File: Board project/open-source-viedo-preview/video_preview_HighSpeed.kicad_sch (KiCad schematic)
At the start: 1 part, among them J6 Conn_01x22_Female

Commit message: 150-200 pin's created by Mateusz
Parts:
- added J15, J16, J5: Conn_01x22_Female, Connector_FFC-FPC:Hirose_FH12-22S-0.5SH_1x22-1MP_P0.50mm_Horizontal, symbol Connector:Conn_01x22_Female
- added J? (x2): HDMI_A_1.4, symbol Connector:HDMI_A_1.4
- added Module?: ComputeModule4-CM4, CM4IO:Raspberry-Pi-4-Compute-Module, symbol RPI_CM4_video_preview:ComputeModule4-CM4
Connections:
- net +3.3V: now also J16.22 (Pin_22)
- net CAM_GPIO: now also J5.17 (Pin_17)
- net GND: now also J15.1 (Pin_1), J15.10 (Pin_10), J15.13 (Pin_13), J15.16 (Pin_16), J15.19 (Pin_19), J15.4 (Pin_4), J15.7 (Pin_7), J16.1 (Pin_1), J16.10 (Pin_10), J16.13 (Pin_13), J16.16 (Pin_16), J16.19 (Pin_19), J16.4 (Pin_4), J16.7 (Pin_7), J5.1 (Pin_1), J5.10 (Pin_10), J5.13 (Pin_13), J5.16 (Pin_16), J5.4 (Pin_4), J5.7 (Pin_7), J?.11 (CKS), J?.11 (CKS), J?.17 (GND), J?.17 (GND), J?.2 (D2S), J?.2 (D2S), J?.5 (D1S), J?.5 (D1S), J?.8 (D0S), J?.8 (D0S), J?.SH, J?.SH
- net SCL0: now also J16.20 (Pin_20)
- net SDA0: now also J16.21 (Pin_21)
- new net: Module?.150 (GND), Module?.156 (GND), Module?.162 (GND), Module?.168 (GND), Module?.174 (GND), Module?.180 (GND), Module?.186 (GND), Module?.192 (GND), Module?.198 (GND)
- new net: Module?.155 (GND), Module?.161 (GND), Module?.167 (GND), Module?.173 (GND), Module?.179 (GND), Module?.185 (GND), Module?.191 (GND), Module?.197 (GND)
- new net +3.3v: J15.22 (Pin_22), J5.22 (Pin_22)
- new net CAM0_D0_N: J5.2 (Pin_2)
- new net CAM0_D0_P: J5.3 (Pin_3)
- new net CAM0_D1_N: J5.5 (Pin_5)
- new net CAM0_D1_P: J5.6 (Pin_6)
- new net CAM0_D2_N: J5.9 (Pin_9)
- new net CAM0_D2_P: J5.8 (Pin_8)
- new net DSI0_C_N: J15.8 (Pin_8), Module?.169 (DSI0_C_N)
- new net DSI0_C_P: J15.9 (Pin_9), Module?.171 (DSI0_C_P)
- new net DSI0_D0_N: J15.2 (Pin_2), Module?.157 (DSI0_D0_N)
- new net DSI0_D0_P: J15.3 (Pin_3)
- new net DSI0_D1_N: J15.5 (Pin_5)
- new net DSI0_D1_P: J15.6 (Pin_6)
- new net DSI1_C_N: J16.8 (Pin_8), Module?.187 (DSI1_C_N)
- new net DSI1_C_P: J16.9 (Pin_9), Module?.189 (DSI1_C_P)
- new net DSI1_D0_N: J16.2 (Pin_2), Module?.175 (DSI1_D0_N)
- new net DSI1_D0_P: Module?.177 (DSI1_D0_P)
- new net DSI1_D1_N: J16.5 (Pin_5), Module?.181 (DSI1_D1_N)
- new net DSI1_D1_P: J16.6 (Pin_6), Module?.183 (DSI1_D1_P)
- new net DSI1_D2_N: J16.11 (Pin_11), Module?.193 (DSI1_D2_N)
- new net DSI1_D2_P: J16.12 (Pin_12), Module?.195 (DSI1_D2_P)
- new net DSI1_D3_N: J16.14 (Pin_14), Module?.194 (DSI1_D3_N)
- new net DSI1_D3_P: J16.15 (Pin_15), Module?.196 (DSI1_D3_P)
- new net DSI1_DO_P: J16.3 (Pin_3)
- new net DSIO_D1_N: Module?.163 (DSI0_D1_N)
- new net DSIO_D1_P: Module?.165 (DSI0_D1_P)
- new net DSIO_DO_P: Module?.159 (DSI0_D0_P)
- new net HDMI0_CEC: J?.13 (CEC), Module?.151 (HDMI0_CEC)
- new net HDMI0_CK_N: J?.12 (CK-), Module?.190 (HDMI0_CLK_N)
- new net HDMI0_CK_P: J?.10 (CK+), Module?.188 (HDMI0_CLK_P)
- new net HDMI0_D0_N: Module?.184 (HDMI0_TX0_N)
- new net HDMI0_D0_P: J?.7 (D0+), Module?.182 (HDMI0_TX0_P)
- new net HDMI0_D1_N: J?.6 (D1-), Module?.178 (HDMI0_TX1_N)
- new net HDMI0_D1_P: J?.4 (D1+), Module?.176 (HDMI0_TX1_P)
- new net HDMI0_D2_N: Module?.172 (HDMI0_TX2_N)
- new net HDMI0_D2_P: J?.1 (D2+), J?.3 (D2-), Module?.170 (HDMI0_TX2_P)
- new net HDMI0_DO_N: J?.9 (D0-)
- new net HDMI0_HOTPLUG: J?.19 (HPD/HEAC-), Module?.153 (HDMI0_HOTPLUG)
- new net HDMI0_SCL: J?.15 (SCL), Module?.200 (HDMI0_SCL)
- new net HDMI0_SDA: J?.16 (SDA), Module?.199 (HDMI0_SDA)
- new net HDMI1_CEC: J?.13 (CEC)
- new net HDMI1_CK_N: J?.12 (CK-), Module?.166 (HDMI1_CLK_N)
- new net HDMI1_CK_P: J?.10 (CK+), Module?.164 (HDMI1_CLK_P)
- new net HDMI1_D0_N: Module?.160 (HDMI1_TX0_N)
- new net HDMI1_D0_P: J?.7 (D0+), Module?.158 (HDMI1_TX0_P)
- new net HDMI1_D1_N: J?.6 (D1-), Module?.154 (HDMI1_TX1_N)
- new net HDMI1_D1_P: J?.4 (D1+), Module?.152 (HDMI1_TX1_P)
- new net HDMI1_D2_P: J?.1 (D2+), J?.3 (D2-)
- new net HDMI1_DO_N: J?.9 (D0-)
- new net HDMI1_HOTPLUG: J?.19 (HPD/HEAC-)
- new net HDMI1_SCL: J?.15 (SCL)
- new net HDMI1_SDA: J?.16 (SDA)
- new net HDMI_5v: J?.18 (+5V), J?.18 (+5V)
- new net SCL1: J15.20 (Pin_20), J5.20 (Pin_20)
- new net SDA1: J15.21 (Pin_21), J5.21 (Pin_21)
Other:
- moved on the sheet: J6

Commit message: pin 101-150
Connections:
- net CAM0_D0_P: now also Module?.130 (CAM0_D0_P)
- net CAM0_D1_N: now also Module?.134 (CAM0_D1_N)
- net CAM0_D1_P: now also Module?.136 (CAM0_D1_P)
- net CAM1_C_N: now also Module?.127 (CAM1_C_N)
- net CAM1_C_P: now also Module?.129 (CAM1_C_P)
- net CAM1_D0_N: now also Module?.115 (CAM1_D0_N)
- net CAM1_D0_P: now also Module?.117 (CAM1_D0_P)
- net CAM1_D1_N: now also Module?.121 (CAM1_D1_N)
- net CAM1_D1_P: now also Module?.123 (CAM1_D1_P)
- net CAM1_D2_N: now also Module?.133 (CAM1_D2_N)
- net CAM1_D2_P: now also Module?.135 (CAM1_D2_P)
- net CAM1_D3_N: now also Module?.139 (CAM1_D3_N)
- net CAM1_D3_P: now also Module?.141 (CAM1_D3_P)
- net GND: now also Module?.107 (GND), Module?.108 (GND), Module?.113 (GND), Module?.114 (GND), Module?.119 (GND), Module?.120 (GND), Module?.125 (GND), Module?.126 (GND), Module?.131 (GND), Module?.132 (GND), Module?.137 (GND), Module?.138 (GND), Module?.144 (GND), Module?.150 (GND), Module?.155 (GND), Module?.156 (GND), Module?.161 (GND), Module?.162 (GND), Module?.167 (GND), Module?.168 (GND), Module?.173 (GND), Module?.174 (GND), Module?.179 (GND), Module?.180 (GND), Module?.185 (GND), Module?.186 (GND), Module?.191 (GND), Module?.192 (GND), Module?.197 (GND), Module?.198 (GND)
- net HDMI1_CEC: now also Module?.149 (HDMI1_CEC)
- net HDMI1_HOTPLUG: now also Module?.143 (HDMI1_HOTPLUG)
- net HDMI1_SCL: now also Module?.147 (HDMI1_SCL)
- net HDMI1_SDA: now also Module?.145 (HDMI1_SDA)
- net USBOTG_ID: now reaches Module?.101 (USB_OTG_ID)
- net PCIE_CLK_nREQ: now reaches Module?.102 (PCIe_CLK_nREQ)
- net USB2_N: now reaches Module?.103 (USB2_N)
- net USB2_P: now reaches Module?.105 (USB2_P)
- net PCIE_nRST: now reaches Module?.109 (PCIe_nRST)
- net PCIE_CLK_P: now reaches Module?.110 (PCIe_CLK_P)
- net PCIE_CLK_N: now reaches Module?.112 (PCIe_CLK_N)
- net PCIE_RX_P: now reaches Module?.116 (PCIe_RX_P)
- net PCIE_RX_N: now reaches Module?.118 (PCIe_RX_N)
- net PCIE_TX_P: now reaches Module?.122 (PCIe_TX_P)
- net PCIE_TX_N: now reaches Module?.124 (PCIe_TX_N)
- net CAM0_DO_N: now reaches Module?.128 (CAM0_D0_N)
- net CAM0_C_N: now reaches Module?.140 (CAM0_C_N)
- net CAM0_C_P: now reaches Module?.142 (CAM0_C_P)
- net HDMI_D2_P: now reaches Module?.146 (HDMI1_TX2_P)
- net HDMI1_D2_N: now reaches Module?.148 (HDMI1_TX2_N)
- no-connect marks 1 -> 4

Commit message: Imporoved electrical schematic
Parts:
- removed Module?: ComputeModule4-CM4, CM4IO:Raspberry-Pi-4-Compute-Module, symbol RPI_CM4_video_preview:ComputeModule4-CM4
- added Module2: ComputeModule4-CM4, CM4IO:Raspberry-Pi-4-Compute-Module, symbol RPI_CM4_video_preview:ComputeModule4-CM4
- gave numbers to parts that had none: 2
- renumbered J5 to J1, J6 to J2, J16 to J3, J15 to J4
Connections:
- net +3.3v is gone; now on net +3V3: J1.22 (Pin_22), J4.22 (Pin_22)
- net CAM0_C_N: now also Module2.140 (CAM0_C_N)
- net CAM0_C_P: now also Module2.142 (CAM0_C_P)
- net CAM0_D0_P: now also Module2.130 (CAM0_D0_P)
- net CAM0_D1_N: now also Module2.134 (CAM0_D1_N)
- net CAM0_D1_P: now also Module2.136 (CAM0_D1_P)
- net CAM0_DO_N: now also Module2.128 (CAM0_D0_N)
- net CAM1_C_N: now also Module2.127 (CAM1_C_N)
- net CAM1_C_P: now also Module2.129 (CAM1_C_P)
- net CAM1_D0_N: now also Module2.115 (CAM1_D0_N)
- net CAM1_D0_P: now also Module2.117 (CAM1_D0_P)
- net CAM1_D1_N: now also Module2.121 (CAM1_D1_N)
- net CAM1_D1_P: now also Module2.123 (CAM1_D1_P)
- net CAM1_D2_N: now also Module2.133 (CAM1_D2_N)
- net CAM1_D2_P: now also Module2.135 (CAM1_D2_P)
- net CAM1_D3_N: now also Module2.139 (CAM1_D3_N)
- net CAM1_D3_P: now also Module2.141 (CAM1_D3_P)
- net DSI0_C_N: now also Module2.169 (DSI0_C_N)
- net DSI0_C_P: now also Module2.171 (DSI0_C_P)
- net DSI0_D0_N: now also Module2.157 (DSI0_D0_N)
- net DSI1_C_N: now also Module2.187 (DSI1_C_N)
- net DSI1_C_P: now also Module2.189 (DSI1_C_P)
- net DSI1_D0_N: now also Module2.175 (DSI1_D0_N)
- net DSI1_D0_P: now also Module2.177 (DSI1_D0_P)
- net DSI1_D1_N: now also Module2.181 (DSI1_D1_N)
- net DSI1_D1_P: now also Module2.183 (DSI1_D1_P)
- net DSI1_D2_N: now also Module2.193 (DSI1_D2_N)
- net DSI1_D2_P: now also Module2.195 (DSI1_D2_P)
- net DSI1_D3_N: now also Module2.194 (DSI1_D3_N)
- net DSI1_D3_P: now also Module2.196 (DSI1_D3_P)
- net DSIO_D1_N: now also Module2.163 (DSI0_D1_N)
- net DSIO_D1_P: now also Module2.165 (DSI0_D1_P)
- net DSIO_DO_P: now also Module2.159 (DSI0_D0_P)
- net GND: now also Module2.107 (GND), Module2.108 (GND), Module2.113 (GND), Module2.114 (GND), Module2.119 (GND), Module2.120 (GND), Module2.125 (GND), Module2.126 (GND), Module2.131 (GND), Module2.132 (GND), Module2.137 (GND), Module2.138 (GND), Module2.144 (GND), Module2.150 (GND), Module2.155 (GND), Module2.156 (GND), Module2.161 (GND), Module2.162 (GND), Module2.167 (GND), Module2.168 (GND), Module2.173 (GND), Module2.174 (GND), Module2.179 (GND), Module2.180 (GND), Module2.185 (GND), Module2.186 (GND), Module2.191 (GND), Module2.192 (GND), Module2.197 (GND), Module2.198 (GND)
- net HDMI0_CEC: now also Module2.151 (HDMI0_CEC)
- net HDMI0_CK_N: now also Module2.190 (HDMI0_CLK_N)
- net HDMI0_CK_P: now also Module2.188 (HDMI0_CLK_P)
- net HDMI0_D0_N: now also Module2.184 (HDMI0_TX0_N)
- net HDMI0_D0_P: now also Module2.182 (HDMI0_TX0_P)
- net HDMI0_D1_N: now also Module2.178 (HDMI0_TX1_N)
- net HDMI0_D1_P: now also Module2.176 (HDMI0_TX1_P)
- net HDMI0_D2_N: now also Module2.172 (HDMI0_TX2_N)
- net HDMI0_D2_P: now also Module2.170 (HDMI0_TX2_P)
- net HDMI0_HOTPLUG: now also Module2.153 (HDMI0_HOTPLUG)
- net HDMI0_SCL: now also Module2.200 (HDMI0_SCL)
- net HDMI0_SDA: now also Module2.199 (HDMI0_SDA)
- net HDMI1_CEC: now also Module2.149 (HDMI1_CEC)
- net HDMI1_CK_N: now also Module2.166 (HDMI1_CLK_N)
- net HDMI1_CK_P: now also Module2.164 (HDMI1_CLK_P)
- net HDMI1_D0_N: now also Module2.160 (HDMI1_TX0_N)
- net HDMI1_D0_P: now also Module2.158 (HDMI1_TX0_P)
- net HDMI1_D1_N: now also Module2.154 (HDMI1_TX1_N)
- net HDMI1_D1_P: now also Module2.152 (HDMI1_TX1_P)
- net HDMI1_D2_N: now also Module2.148 (HDMI1_TX2_N)
- net HDMI1_HOTPLUG: now also Module2.143 (HDMI1_HOTPLUG)
- net HDMI1_SCL: now also Module2.147 (HDMI1_SCL)
- net HDMI1_SDA: now also Module2.145 (HDMI1_SDA)
- net HDMI_D2_P: now also Module2.146 (HDMI1_TX2_P)
- net PCIE_CLK_N: now also Module2.112 (PCIe_CLK_N)
- net PCIE_CLK_P: now also Module2.110 (PCIe_CLK_P)
- net PCIE_CLK_nREQ: now also Module2.102 (PCIe_CLK_nREQ)
- net PCIE_RX_N: now also Module2.118 (PCIe_RX_N)
- net PCIE_RX_P: now also Module2.116 (PCIe_RX_P)
- net PCIE_TX_N: now also Module2.124 (PCIe_TX_N)
- net PCIE_TX_P: now also Module2.122 (PCIe_TX_P)
- net PCIE_nRST: now also Module2.109 (PCIe_nRST)
- net USB2_N: now also Module2.103 (USB2_N)
- net USB2_P: now also Module2.105 (USB2_P)
- net USBOTG_ID: now also Module2.101 (USB_OTG_ID)
- net +3.3V renamed +3V3
- no-connect marks 4 -> 18
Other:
- moved on the sheet: J1, J2, J3, J4, J5, J6

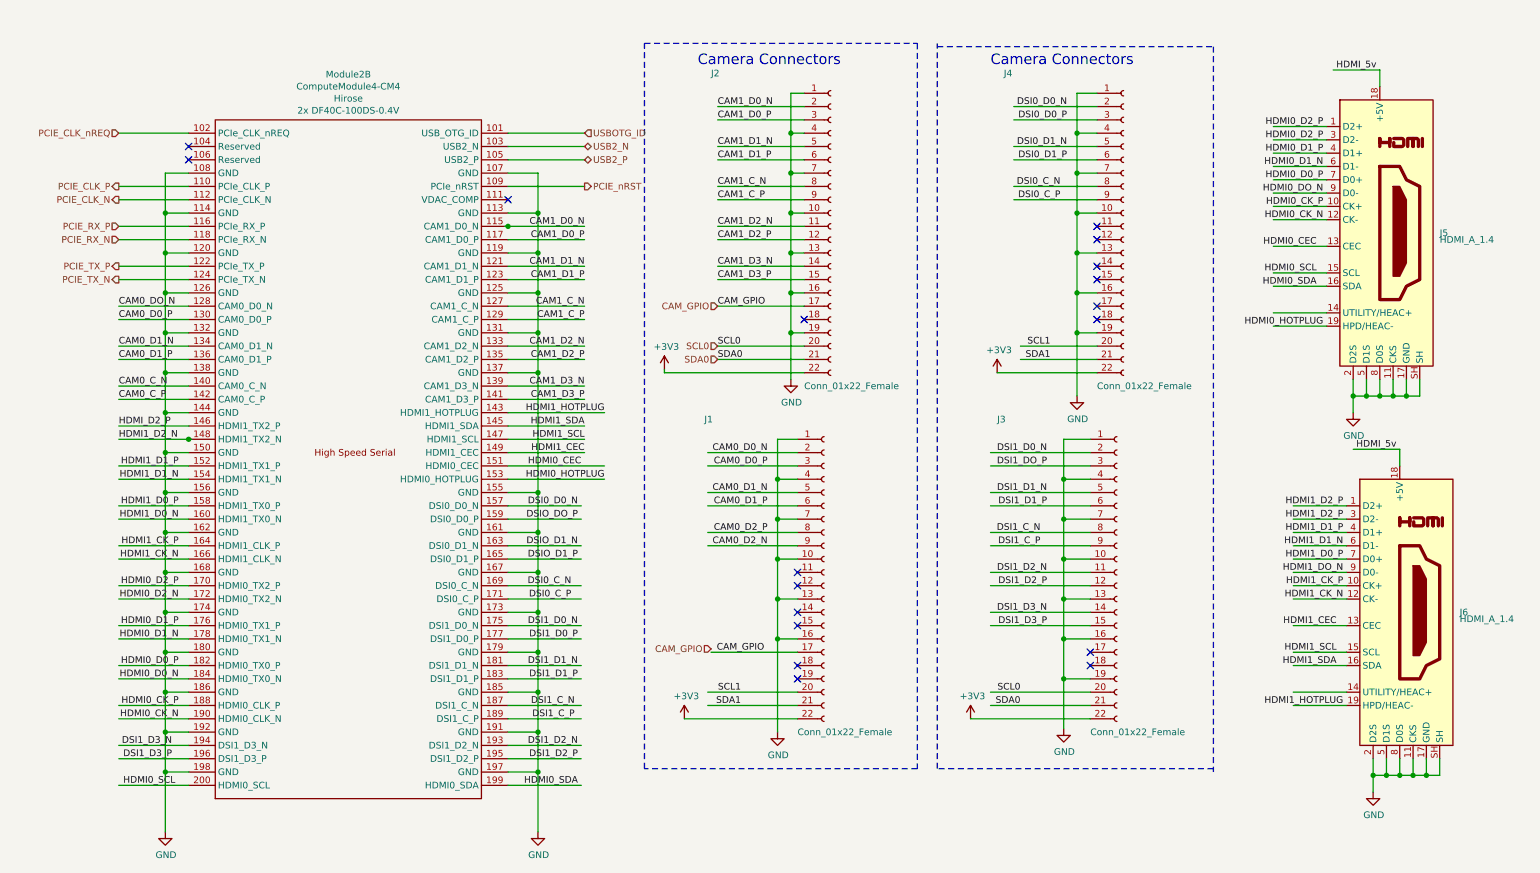
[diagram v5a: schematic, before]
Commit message: ERC error repaired
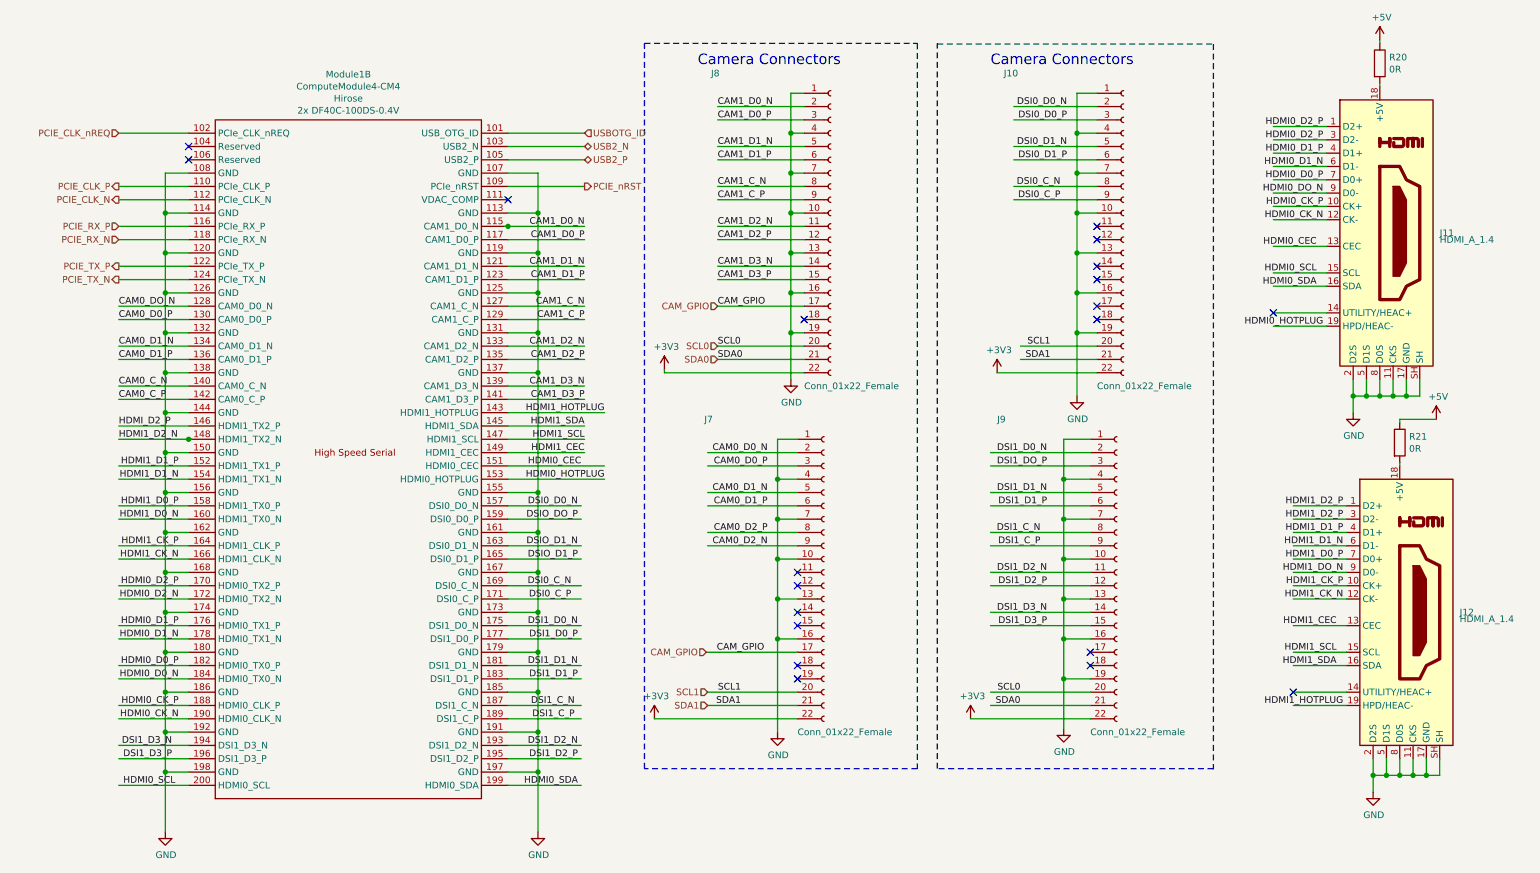
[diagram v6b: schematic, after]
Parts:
- added R20, R21: 0R, symbol Device:R
- renumbered J4 to J10, J5 to J11, J6 to J12, J1 to J7, J2 to J8, J3 to J9, Module2 to Module1
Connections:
- net HDMI_5v: no longer names the net of J11.18 (+5V)
- net HDMI_5v: now also R20.2; no longer J12.18 (+5V)
- new net: J12.18 (+5V), R21.2
- new net +5V: R20.1, R21.1
- no-connect marks 18 -> 20

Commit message: Add HDMI and some power supply paths
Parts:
- J11, J12: footprint (none) -> Connector_HDMI:HDMI_Micro-D_Molex_46765-2x0x
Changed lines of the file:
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@@
       (effects (font (size 1.27 1.27)) (justify left))
     )
-    (property "Footprint" "" (id 2) (at 259.715 54.61 0)
+    (property "Footprint" "Connector_HDMI:HDMI_Micro-D_Molex_46765-2x0x" (id 2) (at 259.715 54.61 0)
       (effects (font (size 1.27 1.27)) hide)
     )
@@
       (effects (font (size 1.27 1.27)) (justify left))
     )
-    (property "Footprint" "" (id 2) (at 263.525 127 0)
+    (property "Footprint" "Connector_HDMI:HDMI_Micro-D_Molex_46765-2x0x" (id 2) (at 263.525 127 0)
       (effects (font (size 1.27 1.27)) hide)
     )
